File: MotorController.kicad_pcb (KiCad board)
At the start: 2 copper layers, 95 x 102.5 mm, 133 parts, among them IC1 ft234xd, IC2 A3921KLPTR-T, IC3 A3921KLPTR-T, J1 SH, J10 PA, J11 XT30, J2 USB_B_Micro, J3 XA, J4 XA, J5 3020-10-0300-00, J6 SH, J7 SH, J8 3020-10-0300-00, J9 XA, Q1 GSFQ6806, Q2 GSFQ6806, Q3 GSFQ6806, Q4 SFS9Z34, Q5 GSFQ6806, Q6 SFS9Z34, SW2 BLACK, SW3 BLACK, SW4 2MS1-T1-B4-VS2-Q-E-S, SW5 RED, U1 LXES11D, U2 STM32F303K8Tx, U3 TJA1441AT, U4 TPSM13604HNDWR, U5 LMZ12002EXT, Y1 32M

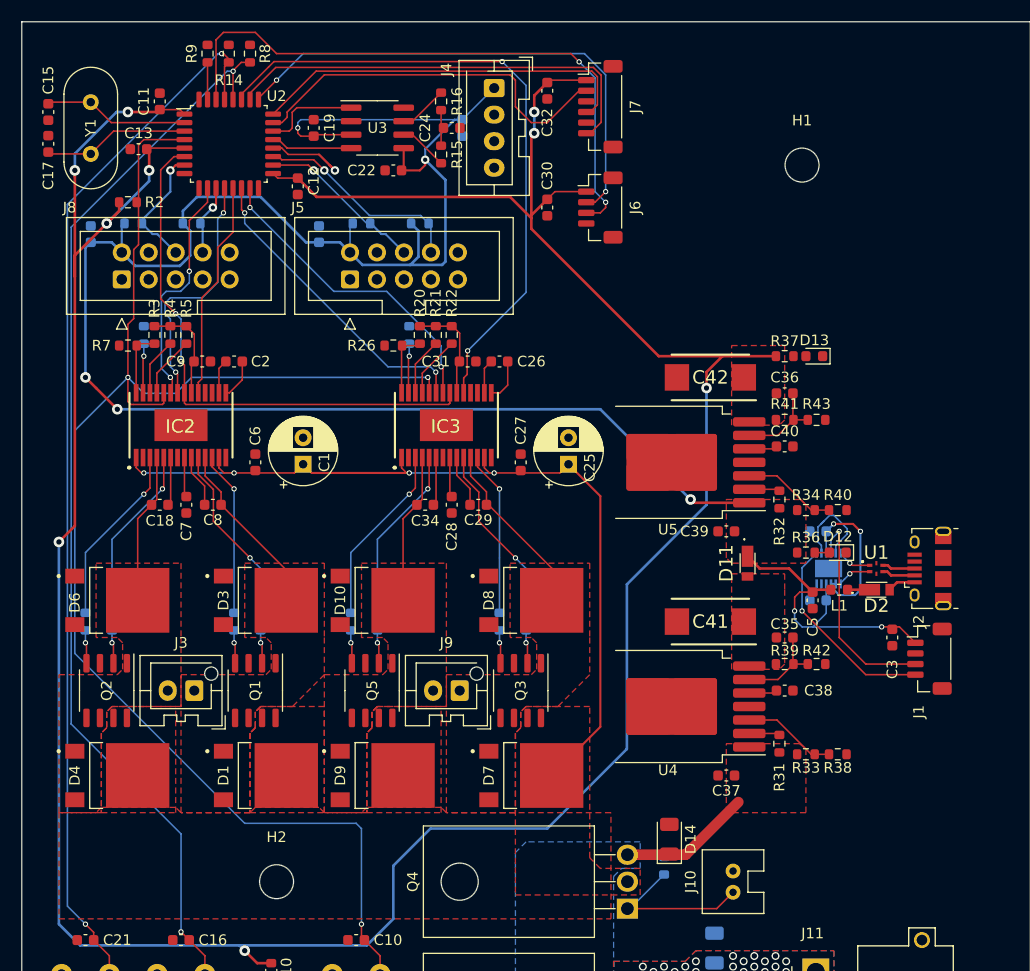
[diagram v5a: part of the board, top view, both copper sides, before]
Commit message: GND 以外の配線をとりあえずやった。水晶の下の配線をなくした。パーツ同士の干渉をなくした。
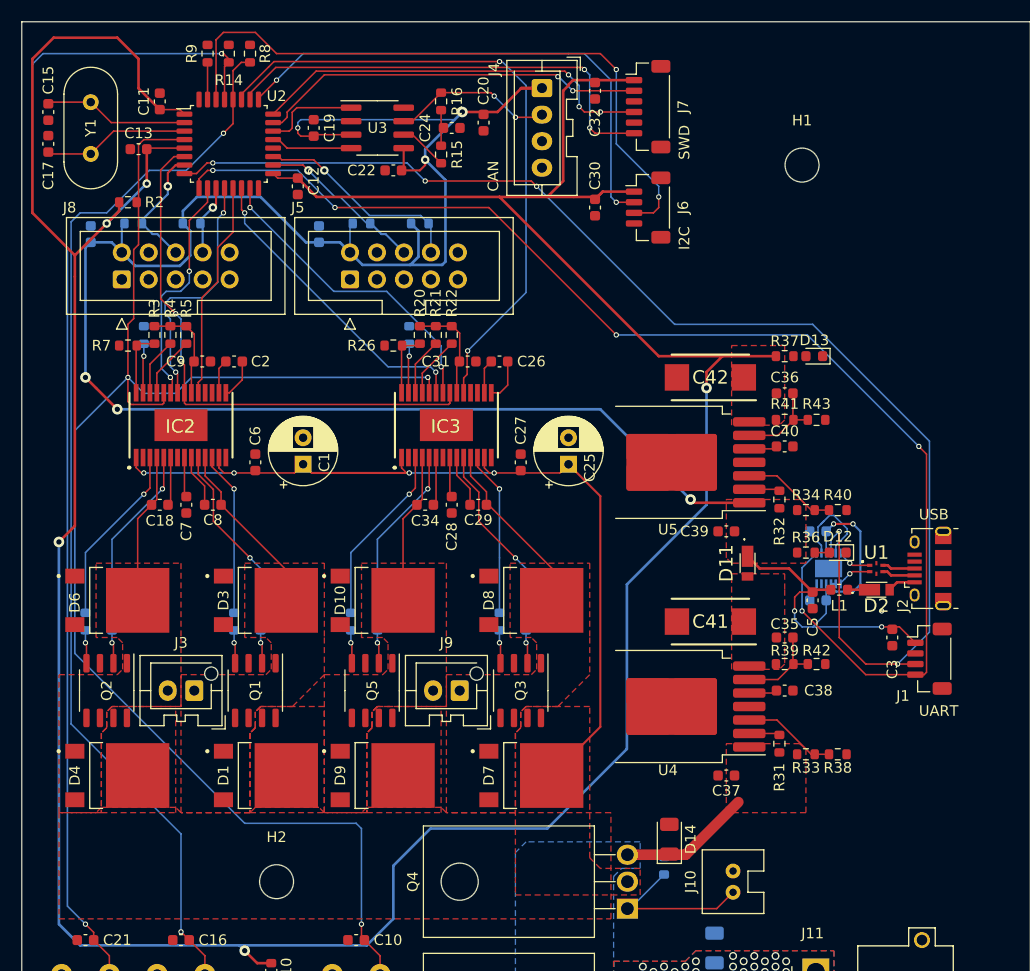
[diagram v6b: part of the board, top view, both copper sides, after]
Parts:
- C20: moved to F.Cu
- moved C30 4.50 mm to (69.0, 32.5)
- moved C32 4.50 mm to (69.0, 21.5)
- moved J4 4.50 mm to (64.0, 21.2)
- moved J6 4.50 mm to (74.0, 32.5)
- moved J7 4.50 mm to (74.0, 23.0)
- moved C20 2.06 mm to (58.5, 24.5)
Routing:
- net Net-(IC1-RXD): track 20.6 -> 124.3 mm, vias 1 -> 5
- net Net-(IC1-TXD): track 19.2 -> 121.7 mm, vias 1 -> 6
- net +3V3: track 294.2 -> 318.2 mm, vias 9 -> 5
- net Net-(U2-PB6): track 105.8 -> 118.2 mm
- net Net-(J4-Pin_2): track 4.64 -> 15.2 mm, vias 0 -> 2
- net Net-(D5-A): track 13.1 -> 3.89 mm, vias 1 -> 0
- net +5V: track 214.0 -> 220.8 mm, vias 7 -> 8
- net Net-(J6-Pin_3): track 58.1 -> 62.3 mm
- net Net-(J7-Pin_4): track 36.4 -> 39.0 mm, vias 0 -> 3
- net Net-(J7-Pin_6): track 41.3 -> 43.3 mm, vias 0 -> 2
- net Net-(J6-Pin_2): track 48.6 -> 49.5 mm
- net Net-(J7-Pin_2): track 36.2 -> 36.8 mm, vias 0 -> 2
- net Net-(IC1-3V3OUT): track 15.3 -> 14.7 mm
- net Net-(U2-PB5): track 108.1 -> 108.6 mm
- net Encoder_LB: vias 2 -> 1
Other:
- board text added: "CAN"
- board text added: "I2C"
- board text added: "SWD"
- board text added: "UART"
- board text added: "USB"

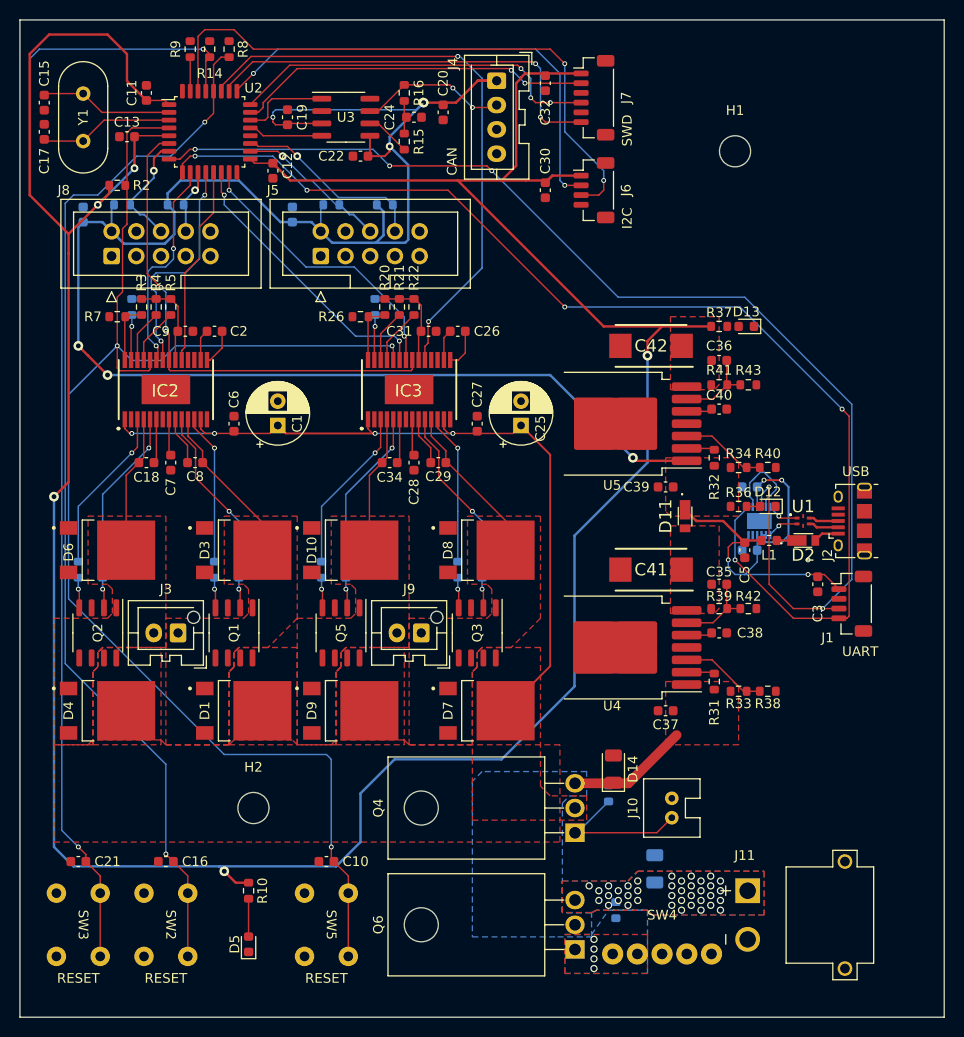
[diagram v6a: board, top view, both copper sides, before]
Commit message: GND アンテナ配線除去中（ビア最大サイズ 0.5 で穴だらけ
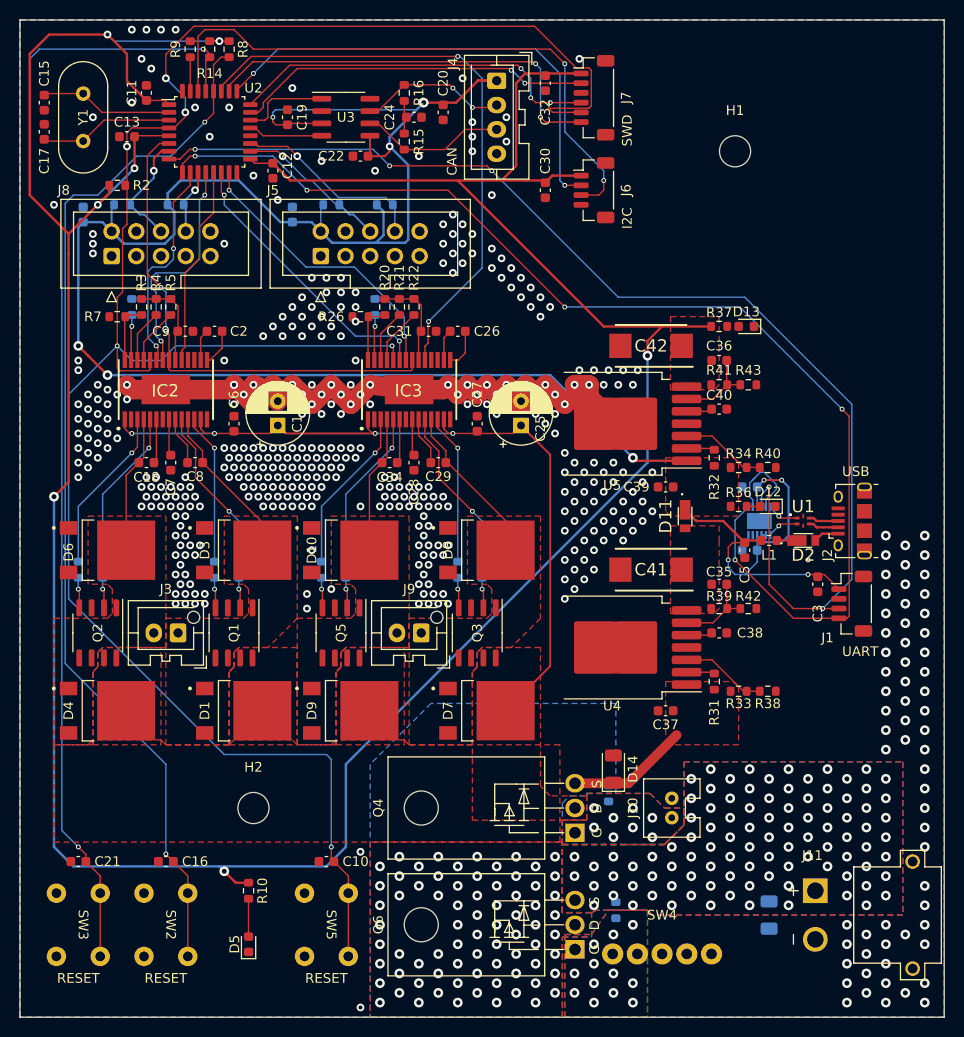
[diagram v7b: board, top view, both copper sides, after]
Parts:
- moved D15 12.7 mm to (92.0, 107.0), turned to -90 degrees
- moved J11 6.96 mm to (106.8, 107.0)
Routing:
- net GND: track 0.00 -> 74.0 mm, vias 0 -> 451
- net NRST: track 147.5 -> 215.4 mm, vias 3 -> 6
- net Net-(J10-Pin_1): track 16.2 -> 1.07 mm, vias 0 -> 8
- net Net-(J4-Pin_3): track 4.64 -> 15.0 mm
- net +3V3: track 318.2 -> 325.0 mm, vias 5 -> 7
- net Net-(D14-K): track 16.9 -> 13.3 mm, vias 0 -> 73
- net Net-(Q6-G): vias 4 -> 12
- net Net-(D15-K): vias 38 -> 95
- added copper zone on B.Cu, net GND
- added copper zone on F.Cu, net GND
- added copper zone on B.Cu, net Net-(J10-Pin_1)
- added copper zone on F.Cu, net Net-(J10-Pin_1)
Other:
- board text added: "10.5A→"
- board text added: "LOGIC↗"
- board text added: "←10.5A"
